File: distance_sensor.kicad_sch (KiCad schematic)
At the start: 31 parts, among them Q3 IRLML6344T, Q4_5 ST-1KL3A, Q4_6 ST-1KL3A, Q4_7 ST-1KL3A, Q4_8 ST-1KL3A

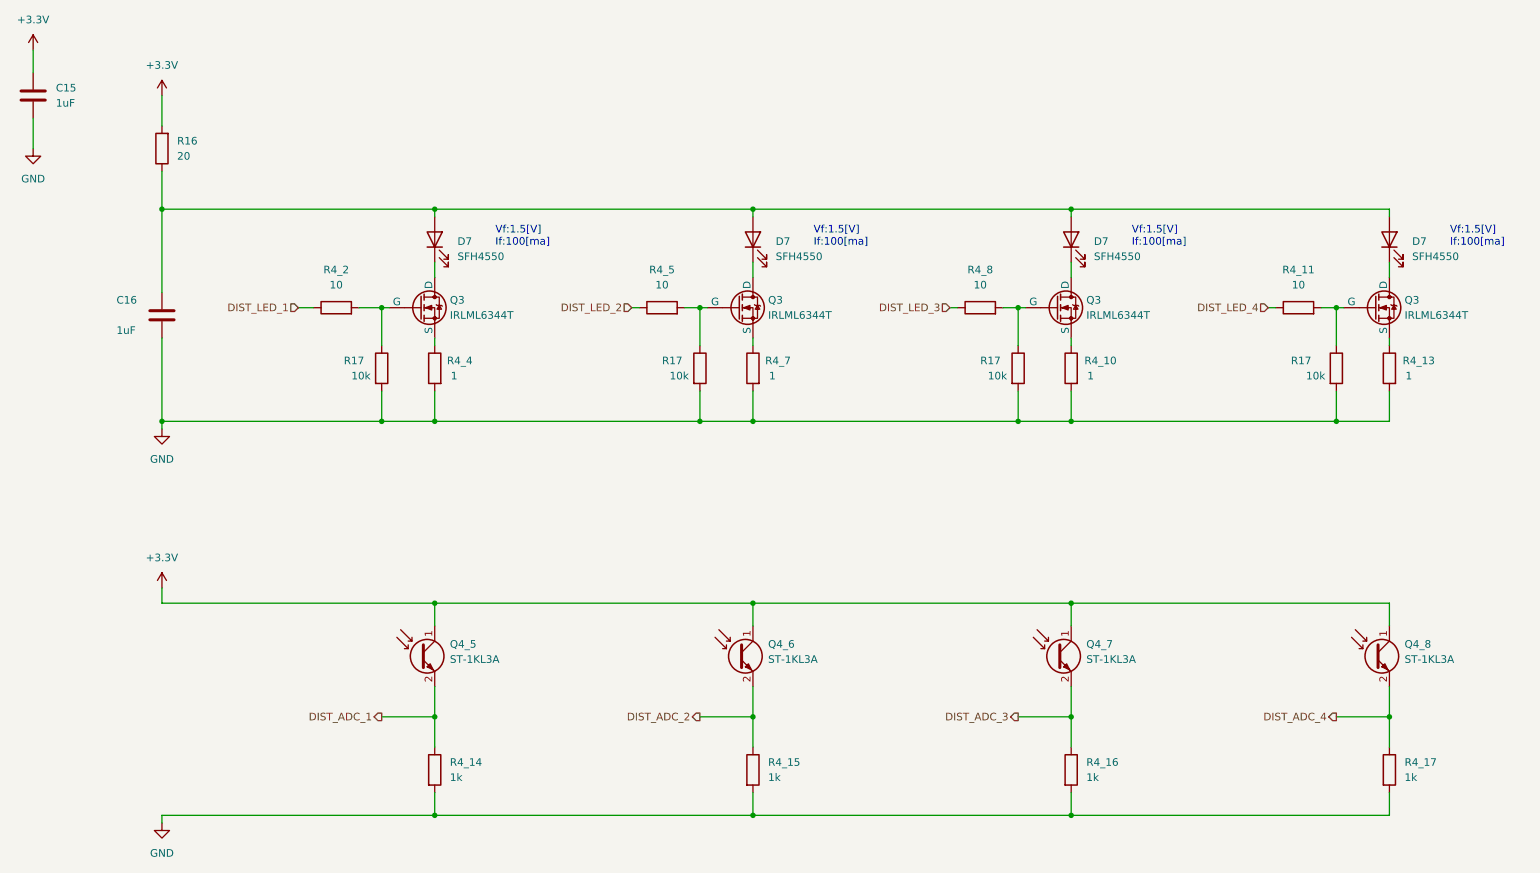
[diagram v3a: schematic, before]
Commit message: 距離センサの制限抵抗をsource側からdrain側に変更
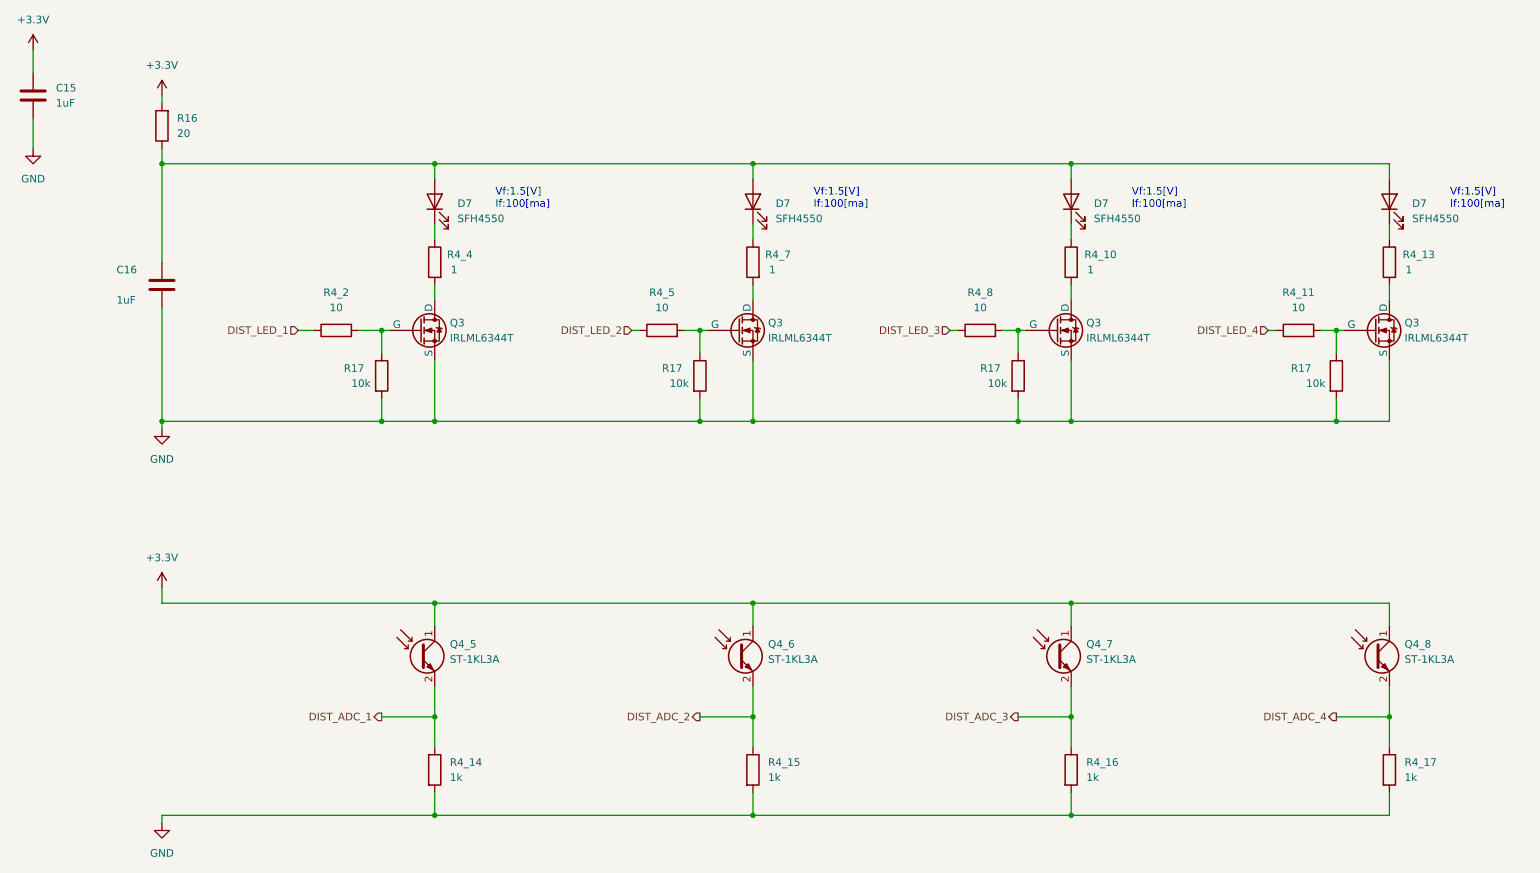
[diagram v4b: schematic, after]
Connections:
- net GND: now also Q3.3 (S), Q3.3 (S), Q3.3 (S), Q3.3 (S); no longer R4_10.2, R4_13.2, R4_4.2, R4_7.2
- net at D7.1 (K): now also R4_4.1; no longer Q3.1 (D)
- net at R4_10.1: now also D7.1 (K); no longer Q3.3 (S)
- net at Q3.1 (D): now also R4_7.2; no longer D7.1 (K)
- net at R4_7.1: now also D7.1 (K); no longer Q3.3 (S)
- net at R4_13.1: now also D7.1 (K); no longer Q3.3 (S)
- net at Q3.1 (D): now also R4_10.2; no longer D7.1 (K)
- net at Q3.1 (D): now also R4_13.2; no longer D7.1 (K)
- new net: Q3.1 (D), R4_4.2
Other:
- moved on the sheet: C16, D7, Q3, R16, R17, R4_11, R4_2, R4_5, R4_8

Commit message: アノテーション番号ミスの修正とフットプリント割り当て途中（部品リストも途中生成）
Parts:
- C15, C16: footprint (none) -> Capacitor_SMD:C_0603_1608Metric_Pad1.08x0.95mm_HandSolder
- D7: footprint (none) -> LED_THT:LED_D5.0mm
- Q3: footprint (none) -> Package_TO_SOT_SMD:SOT-23
- Q4_5, Q4_6, Q4_7, Q4_8: footprint (none) -> Package_TO_SOT_THT:TO-18-2
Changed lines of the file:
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@@
       (effects (font (size 1.27 1.27)) (justify right))
     )
-    (property "Footprint" "" (at 92.71 53.34 0)
+    (property "Footprint" "LED_THT:LED_D5.0mm" (at 92.71 53.34 0)
       (effects (font (size 1.27 1.27)) hide)
     )
@@
       (effects (font (size 1.27 1.27)) (justify left))
     )
-    (property "Footprint" "" (at 148.59 127 0)
+    (property "Footprint" "Package_TO_SOT_THT:TO-18-2" (at 148.59 127 0)
       (effects (font (size 1.27 1.27)) hide)
     )
@@
       (effects (font (size 1.27 1.27)) (justify left))
     )
-    (property "Footprint" "" (at 148.59 72.39 0)
+    (property "Footprint" "Package_TO_SOT_SMD:SOT-23" (at 148.59 72.39 0)
       (effects (font (size 1.27 1.27)) hide)
     )
@@
         )
         (path "/588ca8cd-b11b-4b55-96d9-278aac6cd0cf/dfd8b513-1f63-464b-abba-f89642a821ce"
-          (reference "Q3") (unit 1)
+          (reference "Q4_2") (unit 1)
         )
       )
@@
       (effects (font (size 1.27 1.27)) (justify left))
     )
-    (property "Footprint" "" (at 95.25 127 0)
+    (property "Footprint" "Package_TO_SOT_THT:TO-18-2" (at 95.25 127 0)
       (effects (font (size 1.27 1.27)) hide)
     )
@@
       (effects (font (size 1.27 1.27)) (justify right))
     )
-    (property "Footprint" "" (at 199.39 53.34 0)
+    (property "Footprint" "LED_THT:LED_D5.0mm" (at 199.39 53.34 0)
       (effects (font (size 1.27 1.27)) hide)
     )
@@
       (effects (font (size 1.27 1.27)) (justify left))
     )
-    (property "Footprint" "" (at 47.9552 71.12 0)
+    (property "Footprint" "Capacitor_SMD:C_0603_1608Metric_Pad1.08x0.95mm_HandSolder" (at 47.9552 71.12 0)
       (effects (font (size 1.27 1.27)) hide)
     )
@@
       (effects (font (size 1.27 1.27)) (justify right))
     )
-    (property "Footprint" "" (at 252.73 53.34 0)
+    (property "Footprint" "LED_THT:LED_D5.0mm" (at 252.73 53.34 0)
       (effects (font (size 1.27 1.27)) hide)
     )
@@
         )
         (path "/588ca8cd-b11b-4b55-96d9-278aac6cd0cf/dfd8b513-1f63-464b-abba-f89642a821ce"
-          (reference "Q5") (unit 1)
+          (reference "Q4_4") (unit 1)
         )
       )
@@
       (effects (font (size 1.27 1.27)) (justify left))
     )
-    (property "Footprint" "" (at 201.93 127 0)
+    (property "Footprint" "Package_TO_SOT_THT:TO-18-2" (at 201.93 127 0)
       (effects (font (size 1.27 1.27)) hide)
     )
@@
       (effects (font (size 1.27 1.27)) (justify left))
     )
-    (property "Footprint" "" (at 201.93 72.39 0)
+    (property "Footprint" "Package_TO_SOT_SMD:SOT-23" (at 201.93 72.39 0)
       (effects (font (size 1.27 1.27)) hide)
     )
@@
         )
         (path "/588ca8cd-b11b-4b55-96d9-278aac6cd0cf/dfd8b513-1f63-464b-abba-f89642a821ce"
-          (reference "Q4") (unit 1)
+          (reference "Q4_3") (unit 1)
         )
       )
@@
       (effects (font (size 1.27 1.27)) (justify left))
     )
-    (property "Footprint" "" (at 255.27 127 0)
+    (property "Footprint" "Package_TO_SOT_THT:TO-18-2" (at 255.27 127 0)
       (effects (font (size 1.27 1.27)) hide)
     )
@@
       (effects (font (size 1.27 1.27)) (justify left))
     )
-    (property "Footprint" "" (at 26.3652 39.37 0)
+    (property "Footprint" "Capacitor_SMD:C_0603_1608Metric_Pad1.08x0.95mm_HandSolder" (at 26.3652 39.37 0)
       (effects (font (size 1.27 1.27)) hide)
     )
@@
       (effects (font (size 1.27 1.27)) (justify right))
     )
-    (property "Footprint" "" (at 146.05 53.34 0)
+    (property "Footprint" "LED_THT:LED_D5.0mm" (at 146.05 53.34 0)
       (effects (font (size 1.27 1.27)) hide)
     )
@@
         )
         (path "/588ca8cd-b11b-4b55-96d9-278aac6cd0cf/dfd8b513-1f63-464b-abba-f89642a821ce"
-          (reference "Q2") (unit 1)
-        )
-      )
+          (reference "Q4_1") (unit 1)
+        )
+      )

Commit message: フェライトビーズに型番追加し、自作パッケージの構成へこう
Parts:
- Q3: footprint (none) -> Package_TO_SOT_SMD:SOT-23
- R16, R17, R4_10, R4_11, R4_13, R4_14, R4_15, R4_16, R4_17, R4_2, R4_4, R4_5, R4_7, R4_8: footprint (none) -> Resistor_SMD:R_0603_1608Metric_Pad0.98x0.95mm_HandSolder
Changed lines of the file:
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@@
       (effects (font (size 1.27 1.27)) (justify left))
     )
-    (property "Footprint" "" (at 188.722 82.55 90)
+    (property "Footprint" "Resistor_SMD:R_0603_1608Metric_Pad0.98x0.95mm_HandSolder" (at 188.722 82.55 90)
       (effects (font (size 1.27 1.27)) hide)
     )
@@
       (effects (font (size 1.27 1.27)) (justify left))
     )
-    (property "Footprint" "" (at 144.272 148.59 90)
+    (property "Footprint" "Resistor_SMD:R_0603_1608Metric_Pad0.98x0.95mm_HandSolder" (at 144.272 148.59 90)
       (effects (font (size 1.27 1.27)) hide)
     )
@@
       (effects (font (size 1.27 1.27)) (justify left))
     )
-    (property "Footprint" "" (at 201.168 63.5 90)
+    (property "Footprint" "Resistor_SMD:R_0603_1608Metric_Pad0.98x0.95mm_HandSolder" (at 201.168 63.5 90)
       (effects (font (size 1.27 1.27)) hide)
     )
@@
       (effects (font (size 1.27 1.27)) (justify left))
     )
-    (property "Footprint" "" (at 90.932 148.59 90)
+    (property "Footprint" "Resistor_SMD:R_0603_1608Metric_Pad0.98x0.95mm_HandSolder" (at 90.932 148.59 90)
       (effects (font (size 1.27 1.27)) hide)
     )
@@
       (effects (font (size 1.27 1.27)))
     )
-    (property "Footprint" "" (at 237.49 76.708 90)
+    (property "Footprint" "Resistor_SMD:R_0603_1608Metric_Pad0.98x0.95mm_HandSolder" (at 237.49 76.708 90)
       (effects (font (size 1.27 1.27)) hide)
     )
@@
       (effects (font (size 1.27 1.27)))
     )
-    (property "Footprint" "" (at 130.81 76.708 90)
+    (property "Footprint" "Resistor_SMD:R_0603_1608Metric_Pad0.98x0.95mm_HandSolder" (at 130.81 76.708 90)
       (effects (font (size 1.27 1.27)) hide)
     )
@@
       (effects (font (size 1.27 1.27)) (justify left))
     )
-    (property "Footprint" "" (at 242.062 82.55 90)
+    (property "Footprint" "Resistor_SMD:R_0603_1608Metric_Pad0.98x0.95mm_HandSolder" (at 242.062 82.55 90)
       (effects (font (size 1.27 1.27)) hide)
     )
@@
       (effects (font (size 1.27 1.27)) (justify right))
     )
-    (property "Footprint" "" (at 48.768 40.64 90)
+    (property "Footprint" "Resistor_SMD:R_0603_1608Metric_Pad0.98x0.95mm_HandSolder" (at 48.768 40.64 90)
       (effects (font (size 1.27 1.27)) hide)
     )
@@
       (effects (font (size 1.27 1.27)) (justify left))
     )
-    (property "Footprint" "" (at 250.952 148.59 90)
+    (property "Footprint" "Resistor_SMD:R_0603_1608Metric_Pad0.98x0.95mm_HandSolder" (at 250.952 148.59 90)
       (effects (font (size 1.27 1.27)) hide)
     )
@@
       (effects (font (size 1.27 1.27)) (justify left))
     )
-    (property "Footprint" "" (at 135.382 82.55 90)
+    (property "Footprint" "Resistor_SMD:R_0603_1608Metric_Pad0.98x0.95mm_HandSolder" (at 135.382 82.55 90)
       (effects (font (size 1.27 1.27)) hide)
     )
@@
       (effects (font (size 1.27 1.27)) (justify left))
     )
-    (property "Footprint" "" (at 147.828 63.5 90)
+    (property "Footprint" "Resistor_SMD:R_0603_1608Metric_Pad0.98x0.95mm_HandSolder" (at 147.828 63.5 90)
       (effects (font (size 1.27 1.27)) hide)
     )
@@
       (effects (font (size 1.27 1.27)) (justify left))
     )
-    (property "Footprint" "" (at 255.27 72.39 0)
+    (property "Footprint" "Package_TO_SOT_SMD:SOT-23" (at 255.27 72.39 0)
       (effects (font (size 1.27 1.27)) hide)
     )
@@
       (effects (font (size 1.27 1.27)) (justify left))
     )
-    (property "Footprint" "" (at 82.042 82.55 90)
+    (property "Footprint" "Resistor_SMD:R_0603_1608Metric_Pad0.98x0.95mm_HandSolder" (at 82.042 82.55 90)
       (effects (font (size 1.27 1.27)) hide)
     )
@@
       (effects (font (size 1.27 1.27)) (justify left))
     )
-    (property "Footprint" "" (at 254.508 63.5 90)
+    (property "Footprint" "Resistor_SMD:R_0603_1608Metric_Pad0.98x0.95mm_HandSolder" (at 254.508 63.5 90)
       (effects (font (size 1.27 1.27)) hide)
     )
@@
       (effects (font (size 1.27 1.27)) (justify left))
     )
-    (property "Footprint" "" (at 197.612 148.59 90)
+    (property "Footprint" "Resistor_SMD:R_0603_1608Metric_Pad0.98x0.95mm_HandSolder" (at 197.612 148.59 90)
       (effects (font (size 1.27 1.27)) hide)
     )
@@
       (effects (font (size 1.27 1.27)))
     )
-    (property "Footprint" "" (at 184.15 76.708 90)
+    (property "Footprint" "Resistor_SMD:R_0603_1608Metric_Pad0.98x0.95mm_HandSolder" (at 184.15 76.708 90)
       (effects (font (size 1.27 1.27)) hide)
     )
@@
       (effects (font (size 1.27 1.27)))
     )
-    (property "Footprint" "" (at 76.2 76.708 90)
+    (property "Footprint" "Resistor_SMD:R_0603_1608Metric_Pad0.98x0.95mm_HandSolder" (at 76.2 76.708 90)
       (effects (font (size 1.27 1.27)) hide)
     )
@@
       (effects (font (size 1.27 1.27)) (justify left))
     )
-    (property "Footprint" "" (at 95.25 72.39 0)
+    (property "Footprint" "Package_TO_SOT_SMD:SOT-23" (at 95.25 72.39 0)
       (effects (font (size 1.27 1.27)) hide)
     )
@@
       (effects (font (size 1.27 1.27)) (justify left))
     )
-    (property "Footprint" "" (at 94.488 63.5 90)
-      (effects (font (size 1.27 1.27)) hide)
-    )
+    (property "Footprint" "Resistor_SMD:R_0603_1608Metric_Pad0.98x0.95mm_HandSolder" (at 94.488 63.5 90)
+      (effects (font (size 1.27 1.27)) hide)
+    )

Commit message: 距離センサのフットプリントを修正してpcbまで反映
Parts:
- D7: footprint LED_THT:LED_D5.0mm -> DIstance-Sensor:DIstance-Sensor_LED_D5.0mm
- Q4_5, Q4_6, Q4_7, Q4_8: footprint Package_TO_SOT_THT:TO-18-2 -> DIstance-Sensor:DIstance-Sensor_PHTR_D5.0mm
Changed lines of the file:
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@@
       (effects (font (size 1.27 1.27)) (justify right))
     )
-    (property "Footprint" "LED_THT:LED_D5.0mm" (at 92.71 53.34 0)
+    (property "Footprint" "DIstance-Sensor:DIstance-Sensor_LED_D5.0mm" (at 92.71 53.34 0)
       (effects (font (size 1.27 1.27)) hide)
     )
@@
       (effects (font (size 1.27 1.27)) (justify left))
     )
-    (property "Footprint" "Package_TO_SOT_THT:TO-18-2" (at 148.59 127 0)
+    (property "Footprint" "DIstance-Sensor:DIstance-Sensor_PHTR_D5.0mm" (at 148.59 127 0)
       (effects (font (size 1.27 1.27)) hide)
     )
@@
       (effects (font (size 1.27 1.27)) (justify left))
     )
-    (property "Footprint" "Package_TO_SOT_THT:TO-18-2" (at 95.25 127 0)
+    (property "Footprint" "DIstance-Sensor:DIstance-Sensor_PHTR_D5.0mm" (at 95.25 127 0)
       (effects (font (size 1.27 1.27)) hide)
     )
@@
       (effects (font (size 1.27 1.27)) (justify right))
     )
-    (property "Footprint" "LED_THT:LED_D5.0mm" (at 199.39 53.34 0)
+    (property "Footprint" "DIstance-Sensor:DIstance-Sensor_LED_D5.0mm" (at 199.39 53.34 0)
       (effects (font (size 1.27 1.27)) hide)
     )
@@
       (effects (font (size 1.27 1.27)) (justify right))
     )
-    (property "Footprint" "LED_THT:LED_D5.0mm" (at 252.73 53.34 0)
+    (property "Footprint" "DIstance-Sensor:DIstance-Sensor_LED_D5.0mm" (at 252.73 53.34 0)
       (effects (font (size 1.27 1.27)) hide)
     )
@@
       (effects (font (size 1.27 1.27)) (justify left))
     )
-    (property "Footprint" "Package_TO_SOT_THT:TO-18-2" (at 201.93 127 0)
+    (property "Footprint" "DIstance-Sensor:DIstance-Sensor_PHTR_D5.0mm" (at 201.93 127 0)
       (effects (font (size 1.27 1.27)) hide)
     )
@@
       (effects (font (size 1.27 1.27)) (justify left))
     )
-    (property "Footprint" "Package_TO_SOT_THT:TO-18-2" (at 255.27 127 0)
+    (property "Footprint" "DIstance-Sensor:DIstance-Sensor_PHTR_D5.0mm" (at 255.27 127 0)
       (effects (font (size 1.27 1.27)) hide)
     )
@@
       (effects (font (size 1.27 1.27)) (justify right))
     )
-    (property "Footprint" "LED_THT:LED_D5.0mm" (at 146.05 53.34 0)
-      (effects (font (size 1.27 1.27)) hide)
-    )
+    (property "Footprint" "DIstance-Sensor:DIstance-Sensor_LED_D5.0mm" (at 146.05 53.34 0)
+      (effects (font (size 1.27 1.27)) hide)
+    )
